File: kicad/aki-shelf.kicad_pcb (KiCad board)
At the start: 2 copper layers, 55 x 57.5 mm, 39 parts, among them SW1 RESET, SW10 2x2, SW11 2x3, SW12 1x1, SW13 1x2, SW14 1x3, SW2 UPLOAD, SW3 4x1, SW4 4x2, SW5 4x3, SW6 3x1, SW7 3x2, SW8 3x3, SW9 2x1, U1 NJM2884, U2 AE-FT234X, U3 OPA344NA, U4 AQM0802, U5 ESP-WROOM-32

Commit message: 自動配線を適用
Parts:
- LS1: value Speaker -> UGCT7525AN4
- moved BT1 2.50 mm to (122.3, 81.6)
- moved R1 2.50 mm to (127.3, 91.6), turned to 180 degrees
- moved R6 2.50 mm to (137.3, 74.1)
- moved R7 2.50 mm to (132.3, 74.1)
- moved R8 2.50 mm to (134.8, 74.1)
- moved SW1 2.50 mm to (122.3, 91.6)
- moved SW2 2.50 mm to (122.3, 86.6)
- moved C2 2.00 mm to (137.8, 89.1)
- moved R10 1.50 mm to (140.8, 94.1), turned to 90 degrees
- moved R4 1.50 mm to (140.8, 71.6), turned to 90 degrees
- moved R5 1.50 mm to (140.8, 79.1), turned to 90 degrees
- moved R9 1.50 mm to (140.8, 86.6), turned to 90 degrees
- moved U2 1.41 mm to (128.8, 95.1)
- moved C1 1.00 mm to (129.8, 90.1)
- moved U1 1.00 mm to (133.8, 89.1)
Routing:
- net GND: track 0.00 -> 176.1 mm, vias 0 -> 1
- net +3V3: track 0.00 -> 142.5 mm, vias 0 -> 2
- net TENKEY_C2: track 0.00 -> 98.6 mm, vias 0 -> 2
- net TENKEY_R2: track 0.00 -> 95.1 mm, vias 0 -> 2
- net TENKEY_C3: track 0.00 -> 93.1 mm, vias 0 -> 2
- net TENKEY_R1: track 0.00 -> 87.5 mm
- net TENKEY_R4: track 0.00 -> 78.9 mm, vias 0 -> 2
- net TENKEY_C1: track 0.00 -> 78.2 mm, vias 0 -> 3
- net UART_TX: track 0.00 -> 75.3 mm, vias 0 -> 1
- net UART_RX: track 0.00 -> 74.2 mm, vias 0 -> 1
- net TENKEY_R3: track 0.00 -> 68.2 mm, vias 0 -> 2
- net ENABLE: track 0.00 -> 49.6 mm
- net BAT_VOL: track 0.00 -> 44.1 mm, vias 0 -> 2
- net SPEAKER: track 0.00 -> 36.8 mm
- net LCD_RESET: track 0.00 -> 33.2 mm, vias 0 -> 1
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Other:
- outline, holes or cut-outs redrawn
- board text added: "BT"
- board text added: "GND"
- board text added: "KERI's Lab"
- board text added: "RX"
- board text added: "TX"

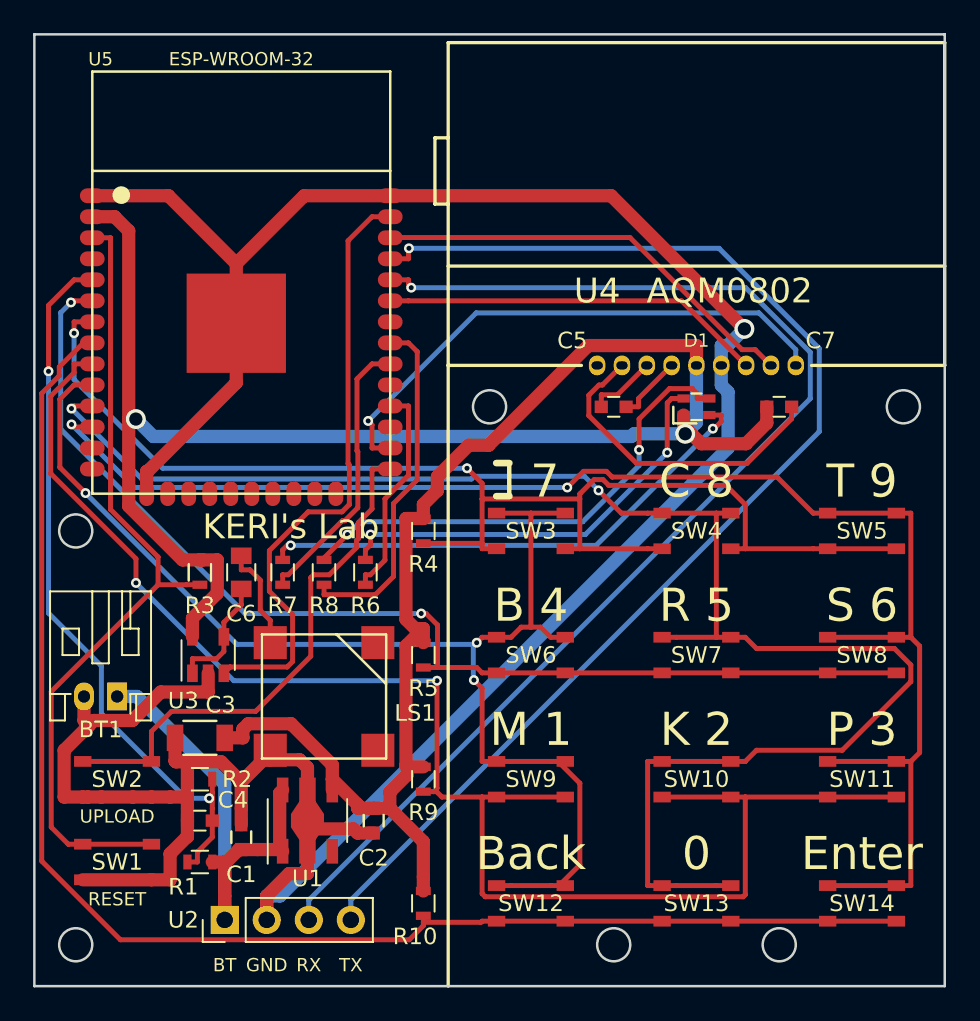
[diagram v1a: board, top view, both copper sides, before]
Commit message: 基板を両面にして小型化
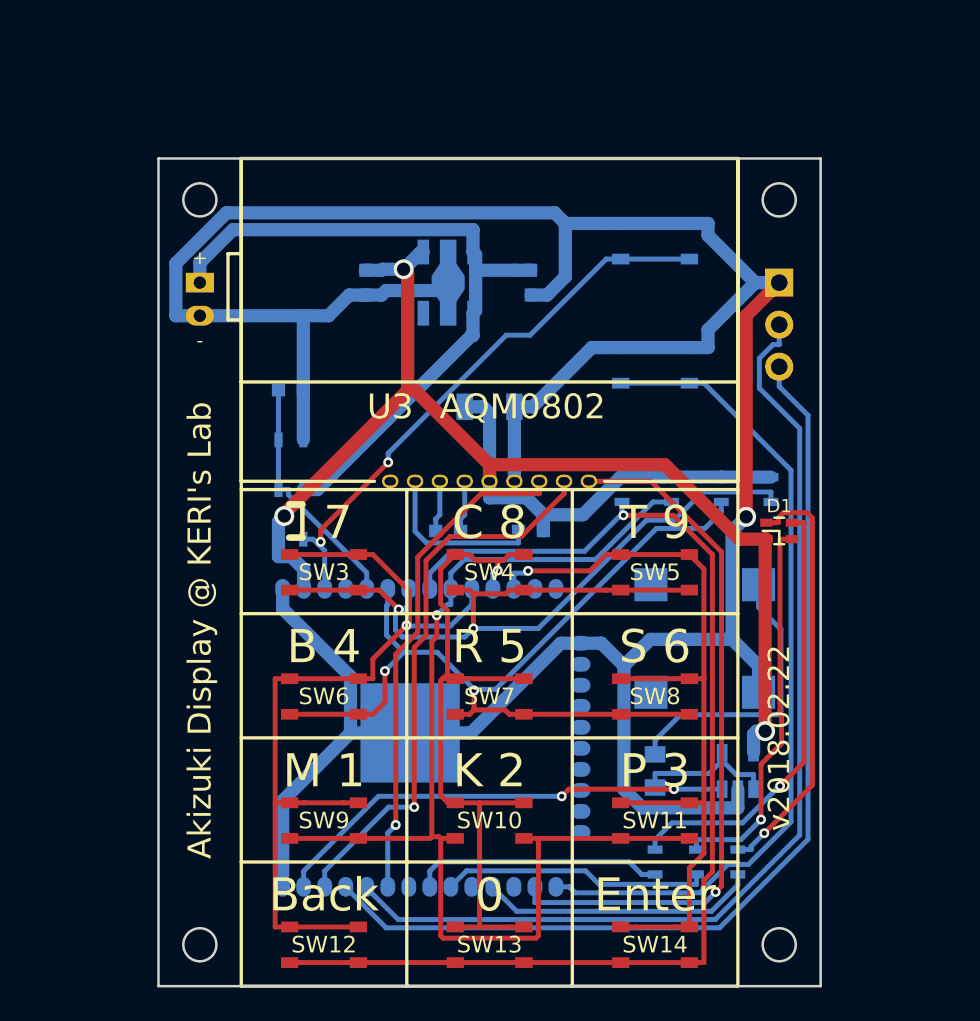
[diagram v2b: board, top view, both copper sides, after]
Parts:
- removed the U2 at (128.8, 95.1)
- added J1: UART, Socket_Strips:Socket_Strip_Straight_1x03_Pitch2.54mm, B.Cu at (162.3, 56.6)
- BT1, C1, C2, C3, C4, C5, C6, C7, LS1, R1, R10, R2, R3, R4, R5, R6, R7, R8, R9, SW1, SW2, U1: moved to B.Cu
- U2: renamed from U3; moved to B.Cu
- U4: renamed from U5; moved to B.Cu
- moved SW1 49.6 mm to (154.8, 54.1)
- moved SW2 41.0 mm to (154.8, 61.6)
- moved C1 37.8 mm to (147.3, 56.6), turned to 270 degrees
- moved U1 33.6 mm to (142.3, 56.6)
- moved U2 32.8 mm to (159.8, 86.1)
- moved C2 32.5 mm to (137.3, 56.6)
- moved R7 30.5 mm to (157.3, 91.6)
- moved U4 28.6 mm to (137.5, 84.1), turned to 90 degrees
- moved R6 28.5 mm to (159.8, 91.6)
- moved C6 27.7 mm to (154.8, 86.1)
- moved R10 27.7 mm to (152.8, 69.1)
- moved C3 26.6 mm to (144.8, 64.1), turned to 0 degrees
- moved R8 26.6 mm to (154.8, 91.6)
- moved C4 26.6 mm to (132.8, 63.1), turned to 0 degrees
- moved BT1 25.5 mm to (127.3, 56.6), turned to 270 degrees
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- renumbered U4 to U3
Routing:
- net TENKEY_C2: track 98.6 -> 43.4 mm, vias 2 -> 1
- net +3V3: track 142.5 -> 93.7 mm, vias 2 -> 3
- net TENKEY_C3: track 93.1 -> 49.4 mm, vias 2 -> 1
- net BAT_VOL: track 44.1 -> 14.6 mm, vias 2 -> 0
- net TENKEY_C1: track 78.2 -> 50.8 mm, vias 3 -> 1
- net TENKEY_R2: track 95.1 -> 69.5 mm, vias 2 -> 1
- net TENKEY_R4: track 78.9 -> 53.6 mm
- net IO0: track 32.0 -> 49.8 mm
- net TENKEY_R1: track 87.5 -> 71.1 mm, vias 0 -> 1
- net ENABLE: track 49.6 -> 34.2 mm, vias 0 -> 2
- net UART_TX: track 75.3 -> 60.5 mm, vias 1 -> 0
- net GND: track 176.1 -> 190.3 mm
- net +5V: track 28.7 -> 42.5 mm
- net TENKEY_R3: track 68.2 -> 54.6 mm
- net UART_RX: track 74.2 -> 61.7 mm, vias 1 -> 0
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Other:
- board size 55 x 57.5 mm -> 40 x 50 mm
- board text added: "+"
- board text added: "-"
- board text added: "Akizuki Display @ KERI's Lab"
- board text added: "v2018.02.22"
- board text removed: "BT"
- board text removed: "KERI's Lab"

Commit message: 穴径を3mmに変更
貼り付けボスが使えるように
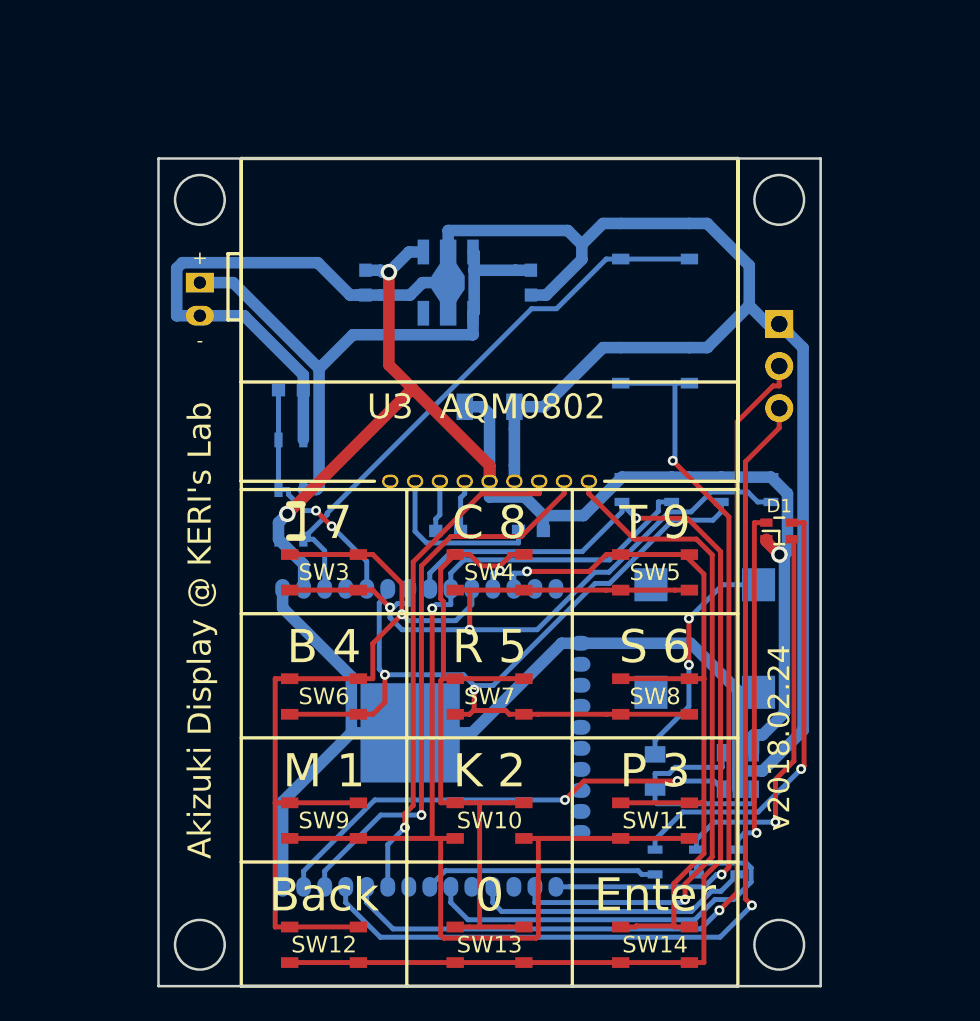
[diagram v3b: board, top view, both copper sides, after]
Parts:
- BT1: value SBH-341-1AS -> JST_PH_S2B-PH-K
- moved J1 2.50 mm to (162.3, 59.1)
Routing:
- net GND: track 190.3 -> 175.0 mm, vias 1 -> 0
- net +3V3: track 93.7 -> 81.1 mm
- net LED_G: track 16.2 -> 25.4 mm
- net +5V: track 42.5 -> 36.2 mm
- net Net-(C6-Pad2): track 8.83 -> 13.7 mm
- net Net-(D1-Pad2): track 25.7 -> 21.4 mm
- net IO0: track 49.8 -> 45.8 mm, vias 0 -> 2
- net UART_RX: track 61.7 -> 58.0 mm, vias 0 -> 1
- net Net-(C6-Pad1): track 17.4 -> 14.1 mm, vias 0 -> 2
- net UART_TX: track 60.5 -> 58.2 mm, vias 0 -> 1
- net LCD_RESET: track 42.6 -> 41.3 mm
- net LED_B: track 15.1 -> 14.1 mm
- net TENKEY_R1: track 71.1 -> 72.0 mm
- net TENKEY_R2: track 69.5 -> 70.2 mm
- net TENKEY_R4: track 53.6 -> 52.9 mm
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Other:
- outline, holes or cut-outs redrawn
- net class 3.3V: trace_width 0.8 -> 0.7; via_dia 1.2 -> 1; via_drill 0.8 -> 0.6
- net class 5V: trace_width 0.8 -> 0.7; via_dia 1.2 -> 1; via_drill 0.8 -> 0.6
- net class GND: trace_width 0.8 -> 0.7; via_dia 1.2 -> 1; via_drill 0.8 -> 0.6
- rule pad_to_mask_clearance: 0.2 -> 0.1
- board text added: "v2018.02.24"
- board text removed: "v2018.02.22"

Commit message: 基板を改良
スイッチの位置，スピーカーの回路など
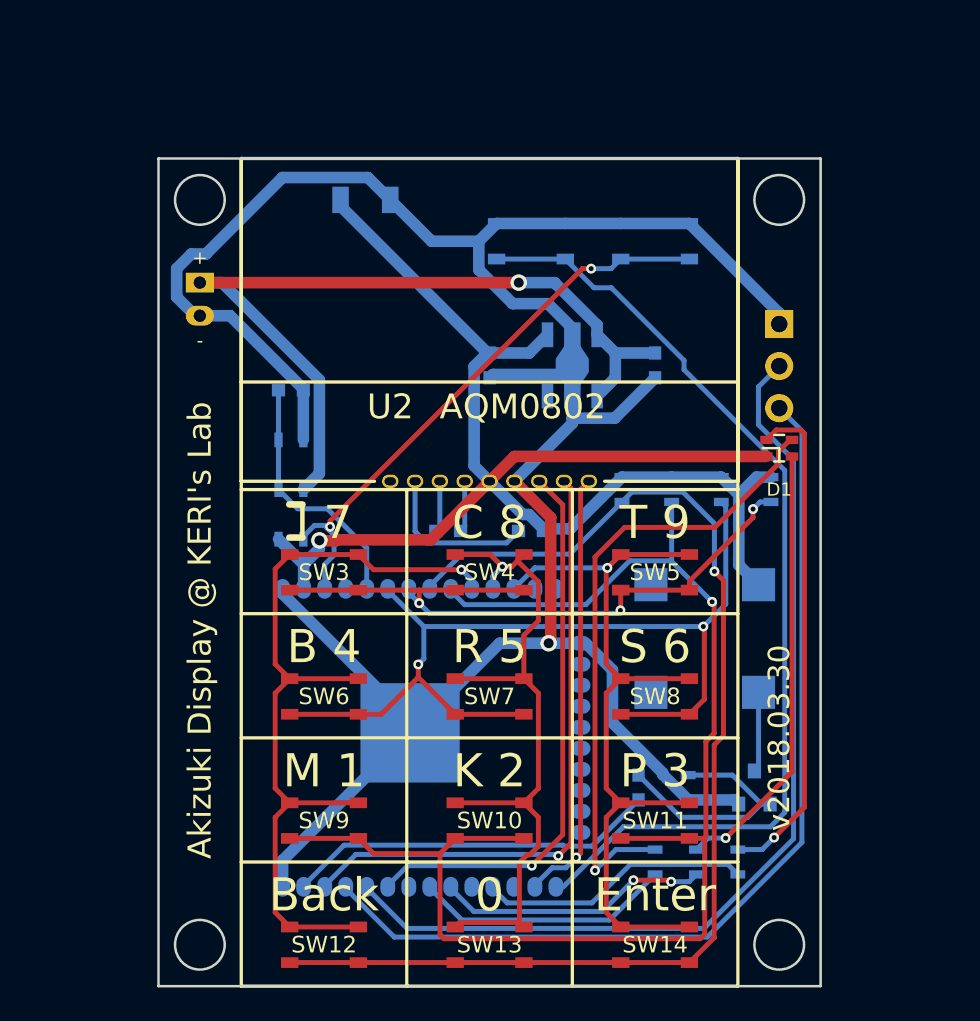
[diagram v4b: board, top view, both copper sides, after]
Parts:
- removed the C6 at (154.8, 86.1)
- removed the U2 at (159.8, 86.1)
- added C7: 0.1u, Capacitors_SMD:C_0603, B.Cu at (153.8, 87.1)
- added Q1: BSS138, TO_SOT_Packages_SMD:SOT-23, B.Cu at (160.8, 87.1)
- added R4: 100k, Resistors_SMD:R_0603, B.Cu at (156.8, 87.1)
- R3: value 10k -> 4.7k
- moved C3 14.6 mm to (137.3, 51.6)
- moved SW2 10.6 mm to (147.3, 54.1)
- moved C1 9.01 mm to (154.8, 61.6)
- moved C2 9.01 mm to (144.8, 61.6)
- moved U1 9.01 mm to (149.8, 61.6)
- moved D1 5.00 mm to (162.3, 66.6)
- renumbered C7 to C6, R9 to R10, R10 to R11, R4 to R5, R5 to R6, R6 to R7, R7 to R8, R8 to R9, U3 to U2, U4 to U3
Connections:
- LS1 pad 1: Net-(C6-Pad1) -> +3V3
- LS1 pad 2: GND -> Net-(LS1-Pad2)
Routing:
- net GND: track 175.0 -> 151.9 mm, vias 0 -> 1
- net LCD_RESET: track 41.3 -> 26.3 mm
- net Net-(C7-Pad1): track 0.00 -> 14.5 mm
- net Net-(C6-Pad1): track 14.1 -> 0.00 mm, vias 2 -> 0
- net Net-(C6-Pad2) (its old number): track 13.7 -> 0.00 mm
- net IO0: track 45.8 -> 59.4 mm, vias 2 -> 0
- net +5V: track 36.2 -> 49.3 mm, vias 0 -> 1
- net TENKEY_R2: track 70.2 -> 83.4 mm
- net Net-(D1-Pad4): track 26.9 -> 38.4 mm
- net TENKEY_R4: track 52.9 -> 41.7 mm, vias 2 -> 3
- net LED_G: track 25.4 -> 16.5 mm, vias 0 -> 2
- net Net-(D1-Pad2): track 21.4 -> 30.3 mm
- net SPEAKER: track 28.7 -> 22.5 mm, vias 2 -> 0
- net +3V3: track 81.1 -> 86.5 mm, vias 3 -> 1
- net Net-(LS1-Pad2): track 0.00 -> 4.85 mm
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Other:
- board text added: "v2018.03.30"
- board text removed: "v2018.02.24"
